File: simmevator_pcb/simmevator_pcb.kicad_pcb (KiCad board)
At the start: 2 copper layers, 3 parts, among them J1 PWR_IN, J2 BUCKREG, U1 XIAO-ESP32-S3-SMD

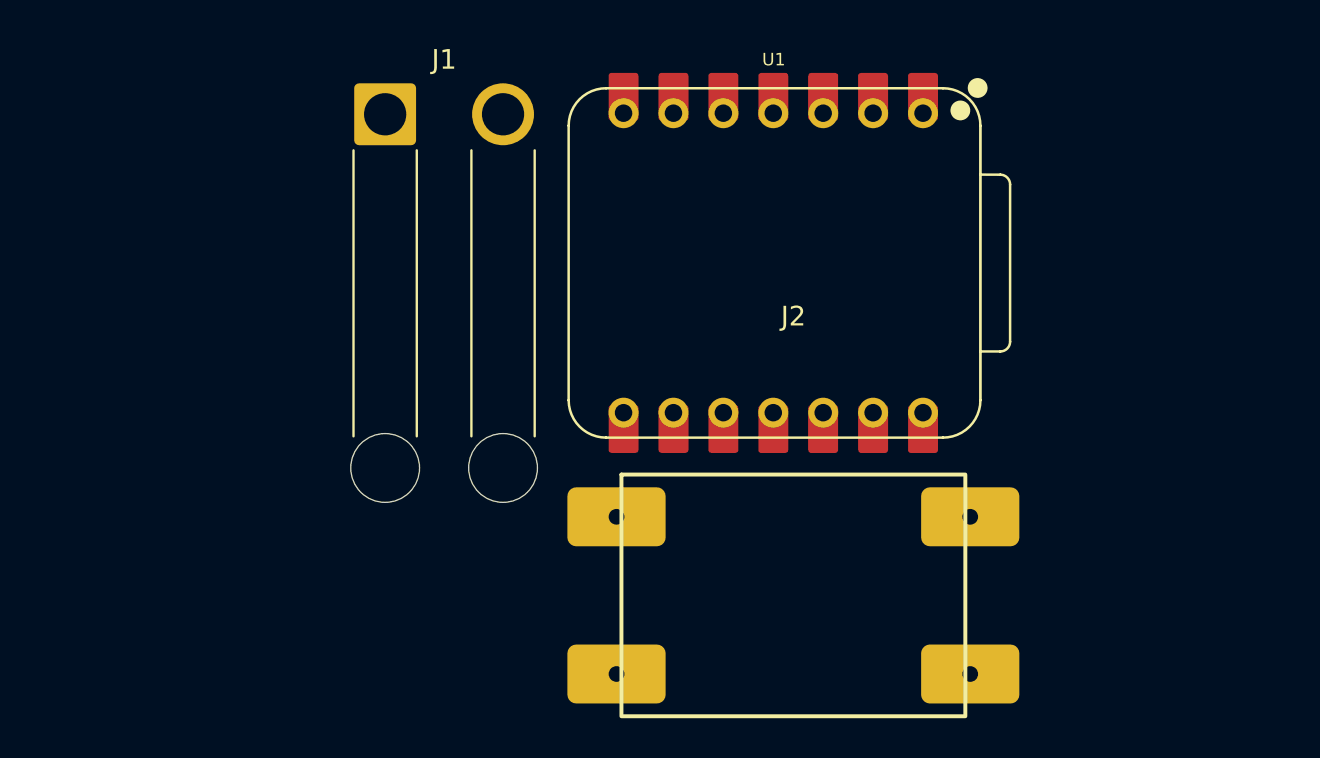
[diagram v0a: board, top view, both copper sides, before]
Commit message: Transmitter schematic: divider, buck header, BMP390 header
Reviewed against docs/HARDWARE.md and it matches the design:

  * R1 100k / R2 20k, tap on U1 pin 1 (D0 = GPIO1 = ADC1_CH0), R1 taken from
    the +12V net that J1 lands on, so the divider reads the pack and not the
    buck. No capacitor across R2, as designed.
  * J2 pin 3 carries +12V into the buck and pin 2 brings +5V back to U1 pin 14
    (VBUS), which is the 5V pad. U1 pin 12 (3V3_OUT) leaves the XIAO as an
    output and only feeds the BMP390 header.
  * J3 pins 3 and 4 to D5/D4 for SCL/SDA, matching platformio.ini.

Unused XIAO pads carry no-connects, so ERC stays quiet about them.

Ignores the analysis/ directory the KiCad analyzer writes.

Co-Authored-By: Claude Opus 5 <noreply@anthropic.com>
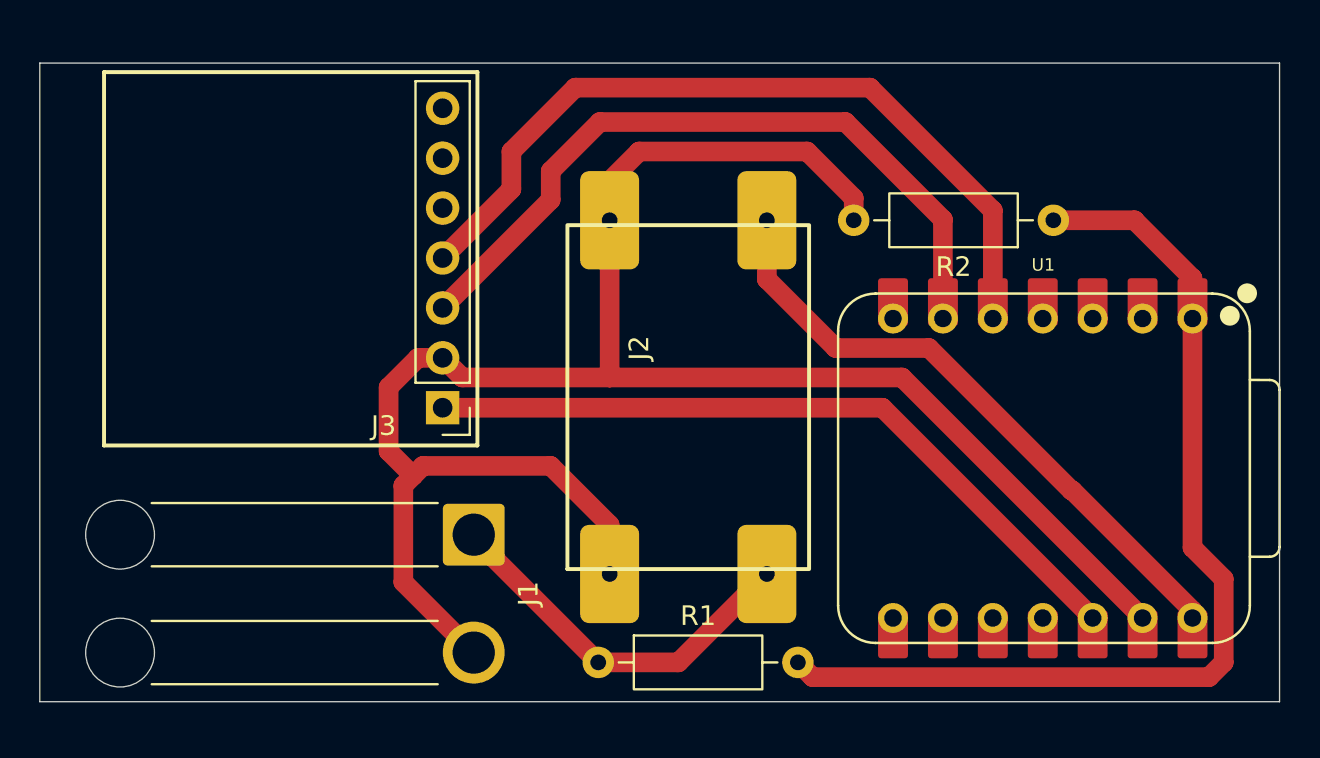
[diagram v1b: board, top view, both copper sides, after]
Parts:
- added J3: BMP390, Connector_PinHeader_2.54mm:PinHeader_1x07_P2.54mm_Vertical, F.Cu at (145.0, 73.0)
- added R1: 100k, Resistor_THT:R_Axial_DIN0207_L6.3mm_D2.5mm_P10.16mm_Horizontal, F.Cu at (152.9, 86.0)
- added R2: 20k, Resistor_THT:R_Axial_DIN0207_L6.3mm_D2.5mm_P10.16mm_Horizontal, F.Cu at (176.1, 63.5)
- moved J1 21.9 mm to (146.6, 79.5), turned to -90 degrees
- moved U1 17.2 mm to (175.5, 76.1)
- moved J2 11.4 mm to (157.5, 72.5), turned to 90 degrees
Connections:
- J2 pad 2: +3V3 -> +5V
- U1 pad 1: unconnected-(U1-D0-Pad1) -> Net-(U1-D0)
- U1 pad 12: unconnected-(U1-3V3_OUT-Pad12) -> +3V3
- U1 pad 13: unconnected-(U1-GND-Pad13) -> GND
- U1 pad 14: unconnected-(U1-VBUS-Pad14) -> +5V
- U1 pad 5: unconnected-(U1-D4-Pad5) -> /SDA
- U1 pad 6: unconnected-(U1-D5-Pad6) -> /SCL
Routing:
- net GND: track 0.00 -> 99.3 mm
- net Net-(U1-D0): track 0.00 -> 50.0 mm
- net /SDA: track 0.00 -> 40.0 mm
- net +3V3: track 0.00 -> 37.5 mm
- net /SCL: track 0.00 -> 36.5 mm
- net +5V: track 0.00 -> 32.9 mm
- net +12V: track 0.00 -> 19.6 mm
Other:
- board outline added: 63.1 x 32.5 mm
